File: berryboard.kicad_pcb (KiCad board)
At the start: 2 copper layers, 56 x 65 mm, 46 parts, among them J1 XT30_SERVO_PWR, J12 QWIIC_RPI_1, J13 QWIIC_RPI_2, J14 QWIIC_RPI_3, J15 QWIIC_MCU_1, J16 QWIIC_MCU_2, J17 QWIIC_MCU_3, J18 LEAK_1, J19 LEAK_2, J2 RPi_GPIO_40P, J20 HAT_5V_IN, J21 SWD, J3 USB_C_RP2350, J4 SERVO_SIG, J5 SERVO_PWR, J6 SERVO_GND, U1 TPS2121, U2 AP2112K-3.3, U3 ICM-42688-P, U4 MMC5983MA, U5 24LC32, U6 RP2350B, U7 W25Q16JVSS

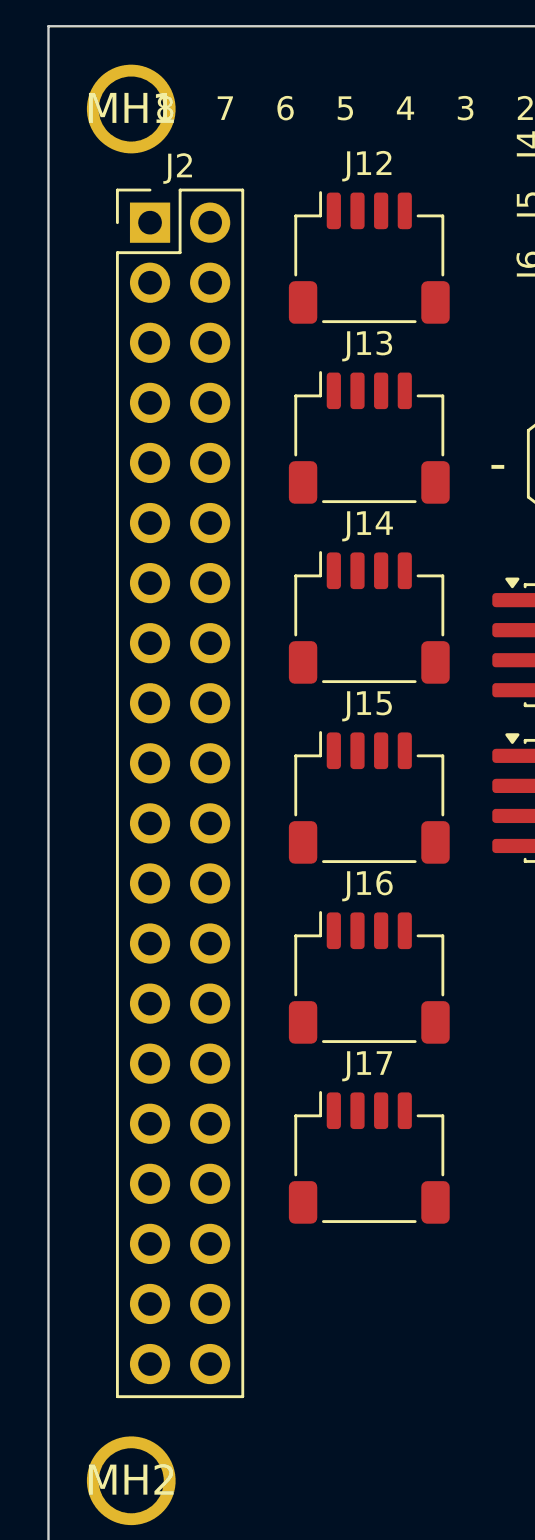
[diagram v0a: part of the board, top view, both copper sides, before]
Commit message: Connector footprint updates: female GPIO socket, vertical QWIIC
J2 (RPi 40-pin GPIO header):
- Footprint: PinHeader_2x20_P2.54mm_Vertical → PinSocket_2x20_P2.54mm_Vertical
- PCB layer: F.Cu → B.Cu (female socket on bottom of board to mate with RPi)
- All F.SilkS/F.Fab/F.CrtYd references flipped to B.* within the footprint block

J12–J17 (six QWIIC/JST-SH connectors):
- Footprint: JST_SH_SM04B-SRSS-TB_1x04-1MP_P1.00mm_Horizontal →
            JST_SH_BM04B-SRSS-TB_1x04-1MP_P1.00mm_Vertical
- Changed in both schematic and PCB

Co-Authored-By: Claude Sonnet 4.6 <noreply@anthropic.com>
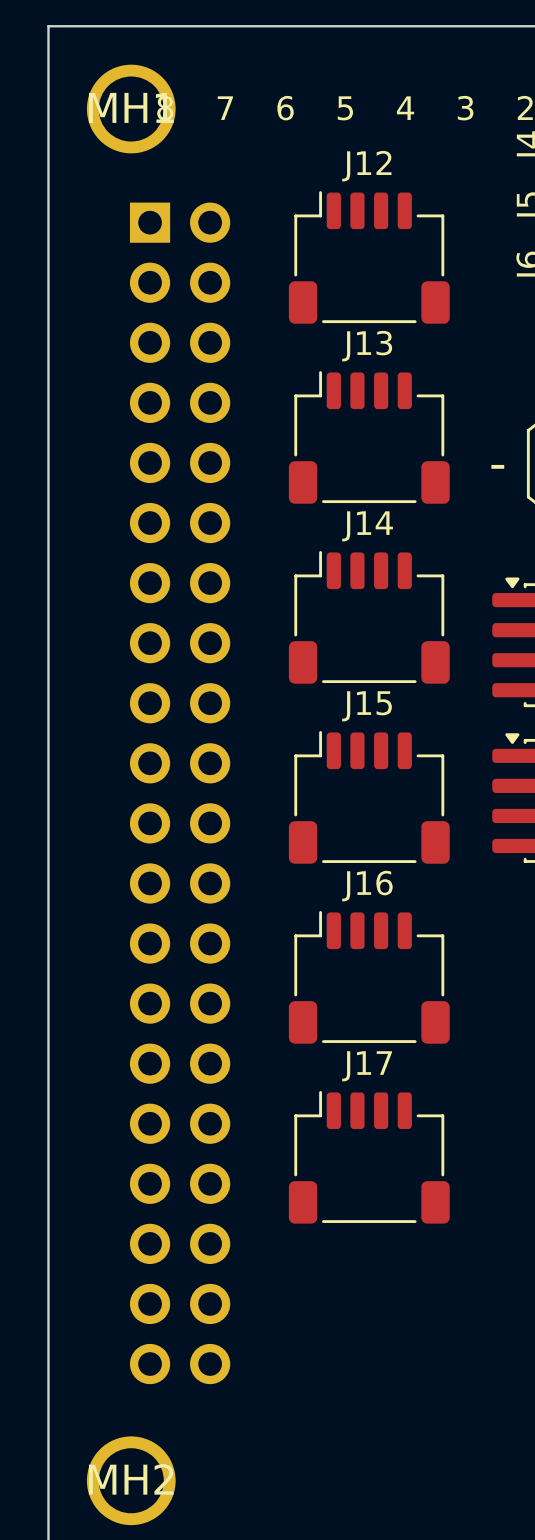
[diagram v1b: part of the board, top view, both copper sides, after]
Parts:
- J12, J13, J14, J15, J16, J17: footprint Connector_JST:JST_SH_SM04B-SRSS-TB_1x04-1MP_P1.00mm_Horizontal -> Connector_JST:JST_SH_BM04B-SRSS-TB_1x04-1MP_P1.00mm_Vertical
- J2: footprint Connector_PinHeader_2.54mm:PinHeader_2x20_P2.54mm_Vertical -> Connector_PinSocket_2.54mm:PinSocket_2x20_P2.54mm_Vertical; moved to B.Cu
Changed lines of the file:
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@@
 		)
 	)
-	(footprint "Connector_PinHeader_2.54mm:PinHeader_2x20_P2.54mm_Vertical"
-		(layer "F.Cu")
+	(footprint "Connector_PinSocket_2.54mm:PinSocket_2x20_P2.54mm_Vertical"
+		(layer "B.Cu")
 		(at 124.795 80.805)
 		(descr "Through hole straight pin header, 2x20, 2.54mm pitch, double rows")
@@
 		(property "Reference" "J2"
 			(at 1.27 -2.38 0)
-			(layer "F.SilkS")
+			(layer "B.SilkS")
 			(effects
 				(font
@@
 		(property "Value" "RPi_GPIO_40P"
 			(at 1.27 50.64 0)
-			(layer "F.Fab")
+			(layer "B.Fab")
 			(effects
 				(font
@@
 		(property "Datasheet" ""
 			(at 0 0 0)
-			(layer "F.Fab")
+			(layer "B.Fab")
 			(hide yes)
 			(effects
@@
 		(property "Description" ""
 			(at 0 0 0)
-			(layer "F.Fab")
+			(layer "B.Fab")
 			(hide yes)
 			(effects
@@
 		(property "KiLib_Generator" "connector/pin_header_socket"
 			(at 0 0 0)
-			(layer "F.SilkS")
+			(layer "B.SilkS")
 			(hide yes)
 			(effects
@@
 				(type solid)
 			)
-			(layer "F.SilkS")
+			(layer "B.SilkS")
 		)
 		(fp_line
@@
 				(type solid)
 			)
-			(layer "F.SilkS")
+			(layer "B.SilkS")
 		)
 		(fp_line
@@
 				(type solid)
 			)
-			(layer "F.SilkS")
+			(layer "B.SilkS")
 		)
 		(fp_line
@@
 				(type solid)
 			)
-			(layer "F.SilkS")
+			(layer "B.SilkS")
 		)
 		(fp_line
@@
 				(type solid)
 			)
-			(layer "F.SilkS")
+			(layer "B.SilkS")
 		)
 		(fp_line
@@
 				(type solid)
 			)
-			(layer "F.SilkS")
+			(layer "B.SilkS")
 		)
 		(fp_line
@@
 				(type solid)
 			)
-			(layer "F.SilkS")
+			(layer "B.SilkS")
 		)
 		(fp_line
@@
 				(type solid)
 			)
-			(layer "F.SilkS")
+			(layer "B.SilkS")
 		)
 		(fp_rect
@@
 			)
 			(fill no)
-			(layer "F.CrtYd")
+			(layer "B.CrtYd")
 		)
 		(fp_line
@@
 				(type solid)
 			)
-			(layer "F.Fab")
+			(layer "B.Fab")
 		)
 		(fp_line
@@
 				(type solid)
 			)
-			(layer "F.Fab")
+			(layer "B.Fab")
 		)
 		(fp_line
@@
 				(type solid)
 			)
-			(layer "F.Fab")
+			(layer "B.Fab")
 		)
 		(fp_line
@@
 				(type solid)
 			)
-			(layer "F.Fab")
+			(layer "B.Fab")
 		)
 		(fp_line
@@
 				(type solid)
 			)
-			(layer "F.Fab")
+			(layer "B.Fab")
 		)
 		(fp_text user "${REFERENCE}"
 			(at 1.27 24.13 90)
-			(layer "F.Fab")
+			(layer "B.Fab")
 			(effects
 				(font
@@
 		)
 	)
-	(footprint "Connector_JST:JST_SH_SM04B-SRSS-TB_1x04-1MP_P1.00mm_Horizontal"
+	(footprint "Connector_JST:JST_SH_BM04B-SRSS-TB_1x04-1MP_P1.00mm_Vertical"
 		(layer "F.Cu")
 		(at 134.065 112.745)
@@
 		)
 		(embedded_fonts no)
-		(model "${KICAD10_3DMODEL_DIR}/Connector_JST.3dshapes/JST_SH_SM04B-SRSS-TB_1x04-1MP_P1.00mm_Horizontal.step"
+		(model "${KICAD10_3DMODEL_DIR}/Connector_JST.3dshapes/JST_SH_BM04B-SRSS-TB_1x04-1MP_P1.00mm_Vertical.step"
 			(offset
 				(xyz 0 0 0)
@@
 		)
 	)
-	(footprint "Connector_JST:JST_SH_SM04B-SRSS-TB_1x04-1MP_P1.00mm_Horizontal"
+	(footprint "Connector_JST:JST_SH_BM04B-SRSS-TB_1x04-1MP_P1.00mm_Vertical"
 		(layer "F.Cu")
 		(at 134.065 120.355)
@@
 		)
 		(embedded_fonts no)
-		(model "${KICAD10_3DMODEL_DIR}/Connector_JST.3dshapes/JST_SH_SM04B-SRSS-TB_1x04-1MP_P1.00mm_Horizontal.step"
+		(model "${KICAD10_3DMODEL_DIR}/Connector_JST.3dshapes/JST_SH_BM04B-SRSS-TB_1x04-1MP_P1.00mm_Vertical.step"
 			(offset
 				(xyz 0 0 0)
@@
 		)
 	)
-	(footprint "Connector_JST:JST_SH_SM04B-SRSS-TB_1x04-1MP_P1.00mm_Horizontal"
+	(footprint "Connector_JST:JST_SH_BM04B-SRSS-TB_1x04-1MP_P1.00mm_Vertical"
 		(layer "F.Cu")
 		(at 134.065 105.135)
@@
 		)
 		(embedded_fonts no)
-		(model "${KICAD10_3DMODEL_DIR}/Connector_JST.3dshapes/JST_SH_SM04B-SRSS-TB_1x04-1MP_P1.00mm_Horizontal.step"
+		(model "${KICAD10_3DMODEL_DIR}/Connector_JST.3dshapes/JST_SH_BM04B-SRSS-TB_1x04-1MP_P1.00mm_Vertical.step"
 			(offset
 				(xyz 0 0 0)
@@
 		(embedded_fonts no)
 	)
-	(footprint "Connector_JST:JST_SH_SM04B-SRSS-TB_1x04-1MP_P1.00mm_Horizontal"
+	(footprint "Connector_JST:JST_SH_BM04B-SRSS-TB_1x04-1MP_P1.00mm_Vertical"
 		(layer "F.Cu")
 		(at 134.065 97.525)
@@
 		)
 		(embedded_fonts no)
-		(model "${KICAD10_3DMODEL_DIR}/Connector_JST.3dshapes/JST_SH_SM04B-SRSS-TB_1x04-1MP_P1.00mm_Horizontal.step"
+		(model "${KICAD10_3DMODEL_DIR}/Connector_JST.3dshapes/JST_SH_BM04B-SRSS-TB_1x04-1MP_P1.00mm_Vertical.step"
 			(offset
 				(xyz 0 0 0)
@@
 		)
 	)
-	(footprint "Connector_JST:JST_SH_SM04B-SRSS-TB_1x04-1MP_P1.00mm_Horizontal"
+	(footprint "Connector_JST:JST_SH_BM04B-SRSS-TB_1x04-1MP_P1.00mm_Vertical"
 		(layer "F.Cu")
 		(at 134.065 82.305)
@@
 		)
 		(embedded_fonts no)
-		(model "${KICAD10_3DMODEL_DIR}/Connector_JST.3dshapes/JST_SH_SM04B-SRSS-TB_1x04-1MP_P1.00mm_Horizontal.step"
+		(model "${KICAD10_3DMODEL_DIR}/Connector_JST.3dshapes/JST_SH_BM04B-SRSS-TB_1x04-1MP_P1.00mm_Vertical.step"
 			(offset
 				(xyz 0 0 0)
@@
 		)
 	)
-	(footprint "Connector_JST:JST_SH_SM04B-SRSS-TB_1x04-1MP_P1.00mm_Horizontal"
+	(footprint "Connector_JST:JST_SH_BM04B-SRSS-TB_1x04-1MP_P1.00mm_Vertical"
 		(layer "F.Cu")
 		(at 134.065 89.915)
@@
 		)
 		(embedded_fonts no)
-		(model "${KICAD10_3DMODEL_DIR}/Connector_JST.3dshapes/JST_SH_SM04B-SRSS-TB_1x04-1MP_P1.00mm_Horizontal.step"
+		(model "${KICAD10_3DMODEL_DIR}/Connector_JST.3dshapes/JST_SH_BM04B-SRSS-TB_1x04-1MP_P1.00mm_Vertical.step"
 			(offset
 				(xyz 0 0 0)

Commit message: Place all design-guide-critical components near U6
Per the RP2350 Hardware Design Guide:

USB resistors (27Ω series on USB_DP/DM):
- R9 → (153.5, 94.0) — 2.8mm from USB_DP pin 67
- R10 → (156.5, 94.0) — 2.8mm from USB_DM pin 66

SMPS switching regulator components:
- L1 (3.3µH Abracon inductor) → (156.24, 91.5) — between VREG_VIN/LX pads
- C2 (4.7µF VREG cap) → (154.5, 90.0) — near L1/VREG pins
- C4 (4.7µF VREG cap) → (158.0, 90.0) — near L1/VREG pins
- R12 (33Ω VREG_AVDD filter) → (159.5, 93.5) — close to VREG_AVDD pin 61
- C15 (4.7µF VREG_AVDD cap) → (159.5, 91.5) — after R12 on filtered rail

Crystal oscillator components:
- C13 (15pF XIN load cap) → (151.0, 108.5) — 3.1mm from XIN pin 30
- C14 (15pF XOUT load cap) → (155.0, 108.5) — 2.5mm from XOUT pin 31
- R11 (1kΩ XOUT series) → (155.5, 110.5) — between XOUT and crystal
- Y1 (12MHz crystal) → (153.44, 114.0) — centered below XIN/XOUT pins

Schematic changes (from prior session):
- Correct FLASH/QSPI labels on U6: FLASH_IO3..IO0, FLASH_CLK, FLASH_CS
  at proper pin positions using correct Y-inversion formula
- Add XIN/XOUT_MCU labels on U6 to connect crystal oscillator circuit
- Add PWR_FLAG on MCU_AVDD net to resolve VREG_AVDD ERC error
- Update L1 footprint to Inductor_SMD:L_Wuerth_PMCI-201610 (same
  2.0x1.6mm body as the Abracon AOTA-B201610S3R3-101-T)
- Sync new components (R9, R10, R11, R12, C13, C14, C15, Y1) to PCB

Co-Authored-By: Claude Sonnet 4.6 <noreply@anthropic.com>
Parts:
- added C12: 100uF, C_1206_3216Metric, F.Cu at (35.6, 20.3)
- added C13: 15pF, C_0402_1005Metric, F.Cu at (151.0, 108.5)
- added C14: 15pF, C_0402_1005Metric, F.Cu at (155.0, 108.5)
- added C15: 4.7uF, C_0402_1005Metric, F.Cu at (159.5, 91.5)
- added D2: SMBJ7.5A, D_SMB, F.Cu at (20.3, 20.3)
- added R10: 27, R_0402_1005Metric, F.Cu at (156.5, 94.0)
- added R11: 1k, R_0402_1005Metric, F.Cu at (155.5, 110.5)
- added R12: 33, R_0402_1005Metric, F.Cu at (159.5, 93.5)
- added R7: 220k, R_0402_1005Metric, F.Cu at (185.4, 129.5)
- added R8: 100k, R_0402_1005Metric, F.Cu at (185.4, 137.2)
- added R9: 27, R_0402_1005Metric, F.Cu at (153.5, 94.0)
- added Y1: ABM8-272-T3, Crystal_SMD_3225-4Pin_3.2x2.5mm, F.Cu at (153.4, 114.0)
- C1, C10, C3, C5, C6, C7, C8, C9: footprint Capacitor_SMD:C_0402_1005Metric -> C_0402_1005Metric
- C11: footprint Capacitor_SMD:C_0805_2012Metric -> C_0805_2012Metric
- C2, C4: value 100nF -> 4.7uF; footprint Capacitor_SMD:C_0402_1005Metric -> C_0402_1005Metric
- D1: footprint LED_SMD:LED_WS2812B_PLCC4_5.0x5.0mm_P3.2mm -> LED_WS2812B_PLCC4_5.0x5.0mm_P3.2mm
- J1: footprint Connector_AMASS:AMASS_XT30UPB-F_1x02_P5.0mm_Vertical -> AMASS_XT30UPB-F_1x02_P5.0mm_Vertical
- J12, J13, J14, J15, J16, J17: footprint Connector_JST:JST_SH_BM04B-SRSS-TB_1x04-1MP_P1.00mm_Vertical -> JST_SH_BM04B-SRSS-TB_1x04-1MP_P1.00mm_Vertical
- J18, J19, J20: footprint Connector_PinHeader_2.54mm:PinHeader_1x02_P2.54mm_Vertical -> PinHeader_1x02_P2.54mm_Vertical
- J2: footprint Connector_PinSocket_2.54mm:PinSocket_2x20_P2.54mm_Vertical -> PinSocket_2x20_P2.54mm_Vertical; moved to F.Cu
- J21: footprint Connector_PinHeader_2.54mm:PinHeader_1x04_P2.54mm_Vertical -> PinHeader_1x04_P2.54mm_Vertical
- J3: footprint Connector_USB:USB_C_Receptacle_HRO_TYPE-C-31-M-12 -> USB_C_Receptacle_HRO_TYPE-C-31-M-12
- J4, J5, J6: footprint Connector_PinHeader_2.54mm:PinHeader_1x08_P2.54mm_Vertical -> PinHeader_1x08_P2.54mm_Vertical
- L1: value 10uH -> AOTA-B201610S3R3-101-T; footprint Inductor_SMD:L_0603_1608Metric -> L_Wuerth_PMCI-201610
- R1, R2, R3, R4, R5, R6: footprint Resistor_SMD:R_0402_1005Metric -> R_0402_1005Metric
- U1: footprint Package_SON:WSON-10-1EP_2.5x2.5mm_P0.5mm_EP1.2x2mm -> WSON-10-1EP_2.5x2.5mm_P0.5mm_EP1.2x2mm
- U2: footprint Package_TO_SOT_SMD:SOT-23-5 -> SOT-23-5
- U3: footprint Package_LGA:LGA-14_3x2.5mm_P0.5mm_LayoutBorder3x4y -> LGA-14_3x2.5mm_P0.5mm_LayoutBorder3x4y
- U4: footprint OptoDevice:Broadcom_LGA-8_2x2mm_P0.5mm -> Broadcom_LGA-8_2x2mm_P0.5mm
- U5, U7: footprint Package_SO:SOIC-8_3.9x4.9mm_P1.27mm -> SOIC-8_3.9x4.9mm_P1.27mm
- U6: footprint Package_DFN_QFN:QFN-80-1EP_10x10mm_P0.4mm_EP3.4x3.4mm -> QFN-80-1EP_10x10mm_P0.4mm_EP3.4x3.4mm
- moved C4 40.6 mm to (158.0, 90.0)
- moved C2 35.7 mm to (154.5, 90.0)
- moved L1 33.0 mm to (156.2, 91.5)
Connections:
- C1 pad 2: /GND -> GND
- C10 pad 2: /GND -> GND
- C2 pad 2: /GND -> GND
- C3 pad 2: /GND -> GND
- C4 pad 2: /GND -> GND
- C5 pad 2: /GND -> GND
- C6 pad 2: /GND -> GND
- C7 pad 2: /GND -> GND
- C8 pad 2: /GND -> GND
- C9 pad 2: /GND -> GND
- D1 pad 3: /GND -> GND
- J1 pad 2: /GND -> GND
- J12 pad 1: /GND -> GND
- J13 pad 1: /GND -> GND
- J14 pad 1: /GND -> GND
- J15 pad 1: /GND -> GND
- J16 pad 1: /GND -> GND
- J17 pad 1: /GND -> GND
- J18 pad 2: /GND -> GND
- J19 pad 2: /GND -> GND
- J2 pad 14: /GND -> GND
- J2 pad 20: /GND -> GND
- J2 pad 25: /GND -> GND
- J2 pad 30: /GND -> GND
- J2 pad 34: /GND -> GND
- J2 pad 39: /GND -> GND
- J2 pad 6: /GND -> GND
- J2 pad 9: /GND -> GND
- J20 pad 2: /GND -> GND
- J21 pad 3: /GND -> GND
- J3 pad A1: /GND -> GND
- J3 pad A12: /GND -> GND
- J3 pad A8: /GND -> GND
- J3 pad B1: /GND -> GND
- J3 pad B12: /GND -> GND
- J3 pad B8: /GND -> GND
- J3 pad SH: /GND -> GND
- J6 pad 1: /GND -> GND
- J6 pad 2: /GND -> GND
- J6 pad 3: /GND -> GND
- J6 pad 4: /GND -> GND
- J6 pad 5: /GND -> GND
- J6 pad 6: /GND -> GND
- J6 pad 7: /GND -> GND
- R1 pad 2: /GND -> GND
- R2 pad 2: /GND -> GND
- U1 pad 5: /GND -> GND
- U1 pad 7: /GND -> GND
- U1 pad 9: /GND -> GND
- U2 pad 2: /GND -> GND
- U3 pad 13: /GND -> GND
- U3 pad 4: /GND -> GND
- U3 pad 7: /GND -> GND
- U3 pad 8: /GND -> GND
- U4 pad 1: /GND -> GND
- U4 pad 2: /GND -> GND
- U5 pad 1: /GND -> GND
- U5 pad 2: /GND -> GND
- U5 pad 3: /GND -> GND
- U5 pad 4: /GND -> GND
- U5 pad 7: /GND -> GND
- U6 pad 30: /GND -> /XIN
- U6 pad 31: unconnected-(U6-XOUT-Pad31) -> /XOUT_MCU
- U6 pad 61: /+3V3 -> /MCU_AVDD
- U6 pad 62: /GND -> GND
- U6 pad 66: /USB_DM -> /USB_DM_MCU
- U6 pad 67: /USB_DP -> /USB_DP_MCU
- U6 pad 81: /GND -> GND
- U7 pad 4: /GND -> GND

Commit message: Manual PCB layout adjustments
Component placement refined by hand in KiCad after initial automated
placement — adjusted positions for better routing, clearance, and
alignment with RP2350 design guide recommendations.

Co-Authored-By: Claude Sonnet 4.6 <noreply@anthropic.com>
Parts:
- J2: moved to B.Cu
- moved D2 135.8 mm to (141.0, 82.5)
- moved C12 119.2 mm to (141.0, 76.0)
- moved U3 30.6 mm to (133.7, 129.2)
- moved R7 28.9 mm to (162.5, 112.0)
- moved R10 28.0 mm to (169.0, 119.0)
- moved R9 28.0 mm to (166.0, 119.0)
- moved R8 27.9 mm to (163.0, 120.5)
- moved J3 26.3 mm to (171.5, 125.5), turned to 90 degrees
- moved U1 20.7 mm to (166.2, 91.5)
- moved L1 17.6 mm to (158.0, 109.0)
- moved U6 16.8 mm to (155.1, 118.1)
- moved R11 15.5 mm to (155.5, 126.0)
- moved C4 15.5 mm to (158.0, 105.5)
- moved C11 12.7 mm to (160.9, 131.0)
- moved U2 12.0 mm to (151.1, 131.0)
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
